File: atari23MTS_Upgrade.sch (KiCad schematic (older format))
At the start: 70 parts, among them P1 CONN_01X01, P10 CONN_01X01, P2 CONN_01X01, P3 CONN_01X01, P4 CONN_01X01, P5 CONN_01X01, P6 CONN_01X01, P7 CONN_01X01, P8 CONN_01X01, P9 CONN_01X01, SW1 SW_PUSH, SW2 SW_PUSH, U1 NCP1117ST33T3G, U2 STM32F401RCTx, U3 NCP1117ST33T3G, U4 STM32F401RCTx

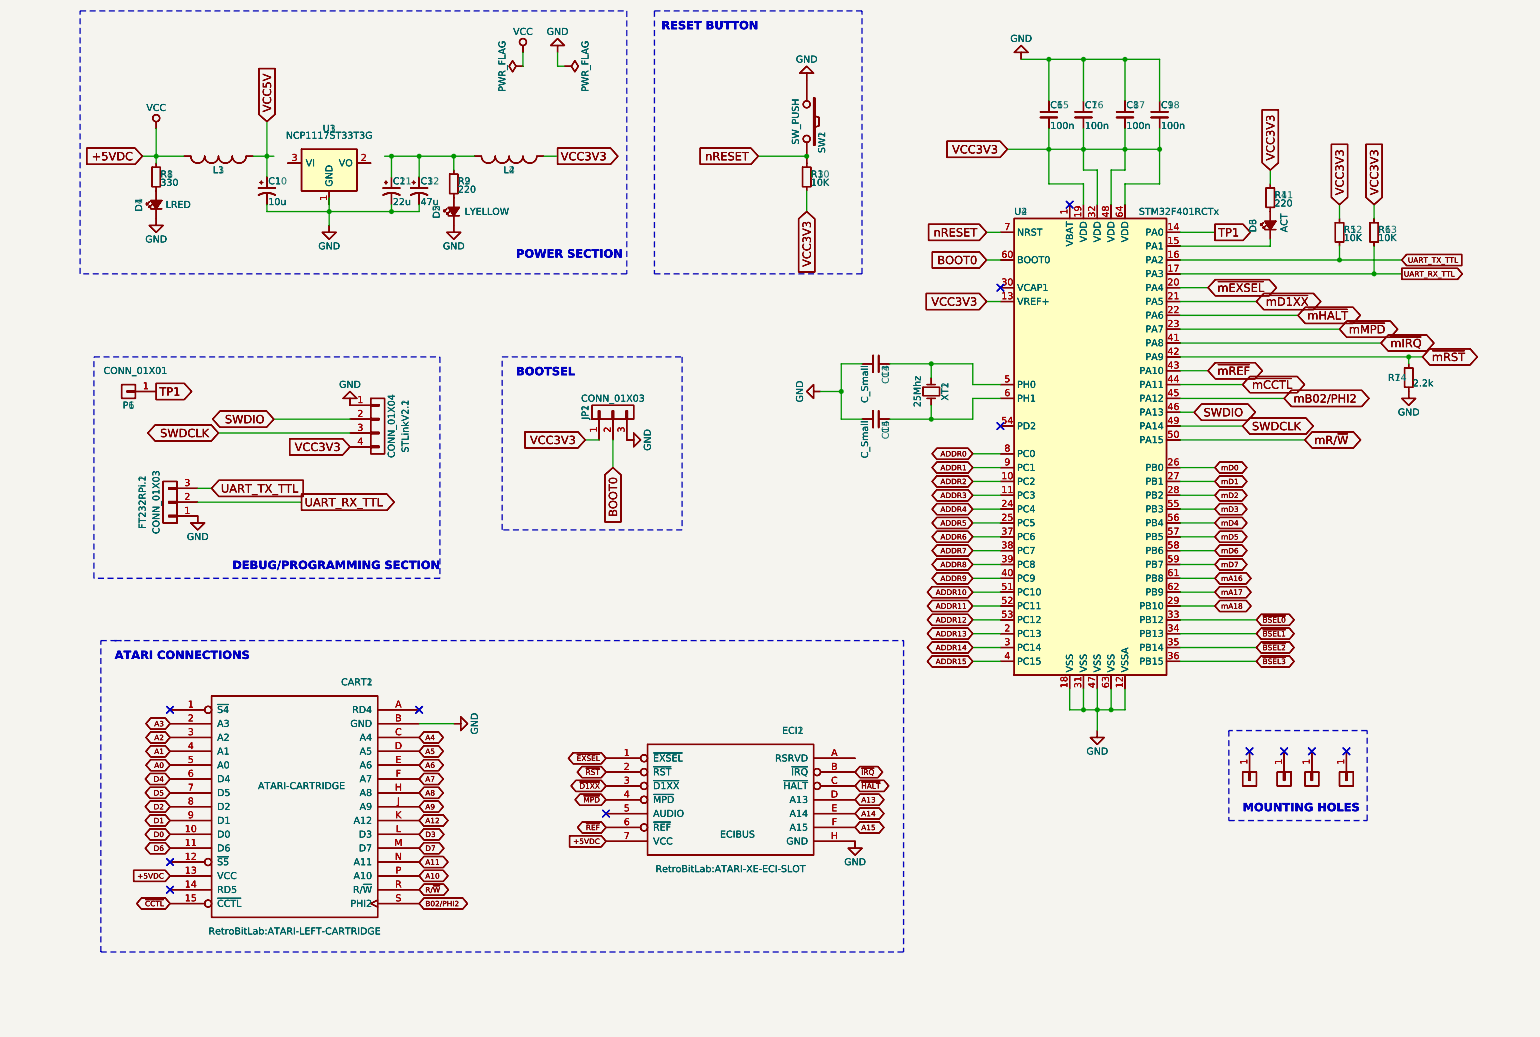
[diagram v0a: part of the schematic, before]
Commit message: added some footprint and revised logic for address selection
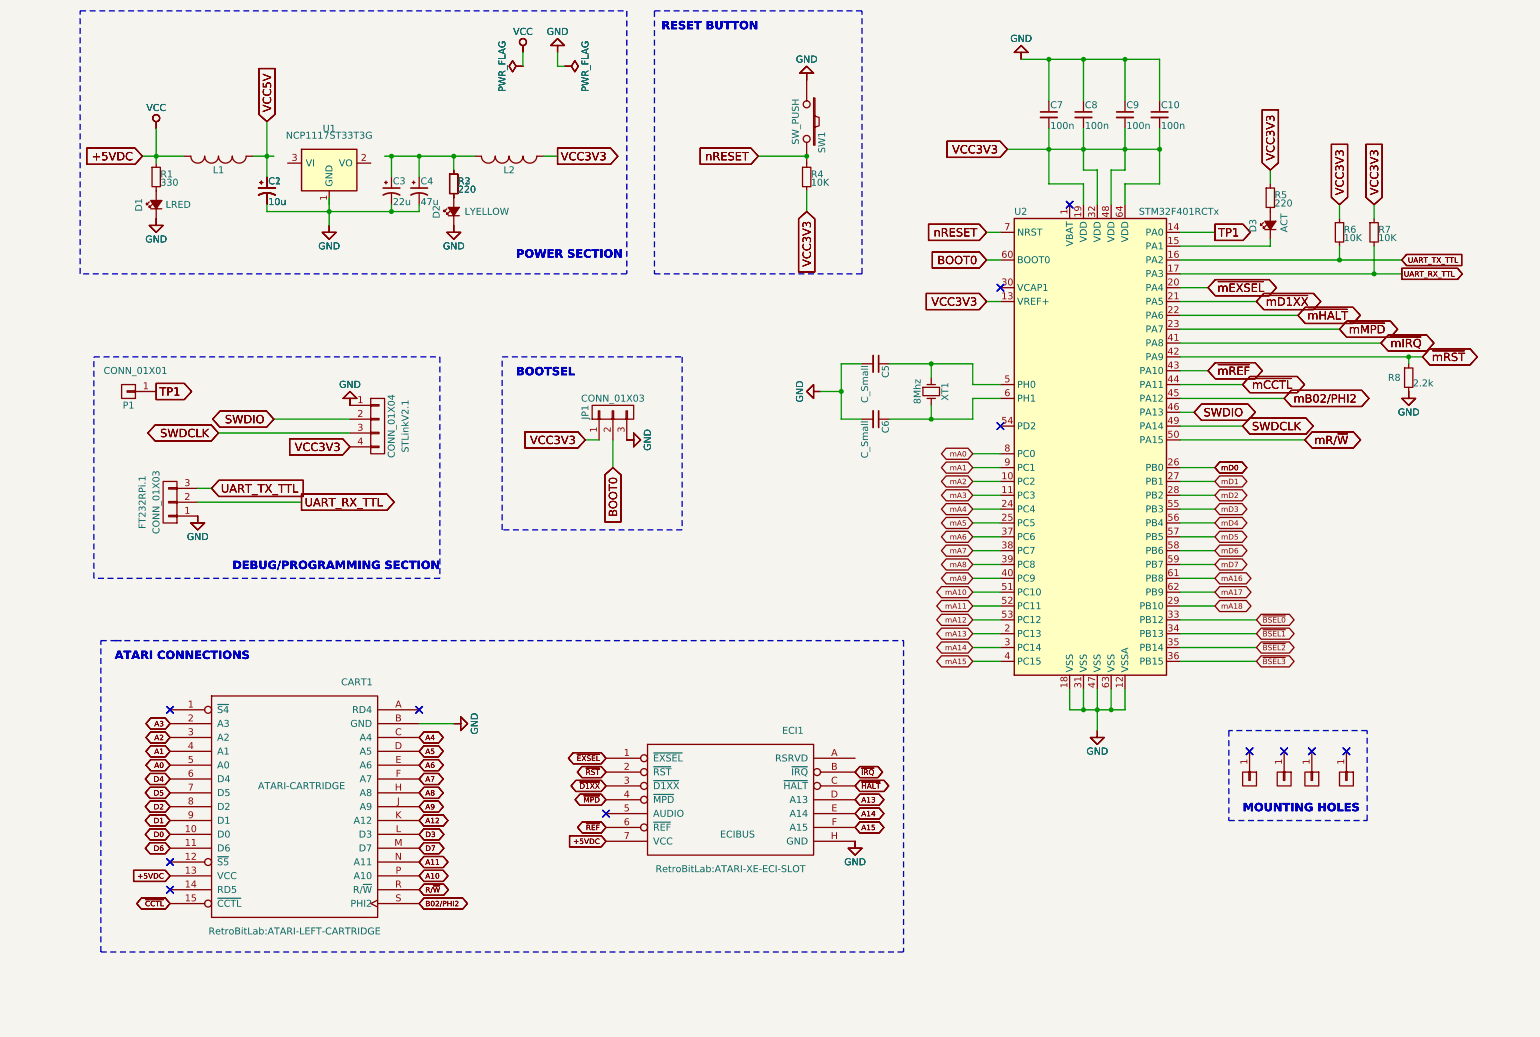
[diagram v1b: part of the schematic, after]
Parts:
- removed C11: 22u, Capacitors_SMD:c_elec_5x5.3, symbol CP1_Small
- removed C3: 47u, Capacitors_SMD:c_elec_5x5.3, symbol CP1_Small
- removed C4, C5: C_Small, Capacitors_SMD:C_1206_HandSoldering, symbol C_Small
- removed C6, C7, C8, C9: 100n, Capacitors_SMD:C_1206_HandSoldering, symbol C_Small
- removed CART1: ATARI-CARTRIDGE, RetroBitLab:ATARI-LEFT-CARTRIDGE, symbol ATARICARTRIDGE
- removed D1: LRED, LEDs:LED_1206, symbol Led_Small
- removed D2: LYELLOW, LEDs:LED_1206, symbol Led_Small
- removed D3: ACT, LEDs:LED_1206, symbol Led_Small
- removed ECI1: ECIBUS, RetroBitLab:ATARI-XE-ECI-SLOT, symbol ECIBUS
- removed FT232RPi.1, JP1: CONN_01X03, Pin_Headers:Pin_Header_Straight_1x03, symbol CONN_01X03
- removed L1, L2: INDUCTOR_SMALL, Choke_SMD:Choke_SMD_1206_Handsoldering, symbol INDUCTOR_SMALL
- removed P1: CONN_01X01, Measurement_Points:Measurement_Point_Round-SMD-Pad_Small, symbol CONN_01X01
- removed P2, P3, P4, P5: CONN_01X01, Connect:1pin, symbol CONN_01X01
- removed R1: 330, Resistors_SMD:R_1206_HandSoldering, symbol R_Small
- removed R3, R5, R6: 10K, Resistors_SMD:R_1206_HandSoldering, symbol R_Small
- removed R4: 220, Resistors_SMD:R_1206_HandSoldering, symbol R_Small
- removed R7: 2.2k, Resistors_SMD:R_1206_HandSoldering, symbol R_Small
- removed STLinkV2.1: CONN_01X04, Pin_Headers:Pin_Header_Angled_1x04, symbol CONN_01X04
- removed SW1: SW_PUSH, Buttons_Switches_SMD:SW_SPST_FSMSM, symbol SW_PUSH
- removed U1: NCP1117ST33T3G, TO_SOT_Packages_SMD:SOT-223, symbol NCP1117ST33T3G
- removed U2: STM32F401RCTx, Housings_QFP:LQFP-64_10x10mm_Pitch0.5mm, symbol STM32F401RCTx
- removed XT1: 25Mhz, Crystals:Crystal_SMD_0603_4Pads, symbol Crystal_Small
- XT1: renamed from XT2; value 25Mhz -> 8Mhz
- renumbered C18 to C10, C10 to C2, C2 to C3, C12 to C4, C13 to C5, C14 to C6, C15 to C7, C16 to C8, C17 to C9, CART2 to CART1, D4 to D1, D5 to D2, D6 to D3, ECI2 to ECI1, FT232RPi.2 to FT232RPi.1, JP2 to JP1, L3 to L1, L4 to L2, P6 to P1, P7 to P2, P8 to P3, P9 to P4, P10 to P5, R8 to R1, R9 to R3, R10 to R4, R11 to R5, R12 to R6, R13 to R7, R14 to R8, STLinkV2.2 to STLinkV2.1, SW2 to SW1, U3 to U1, U4 to U2
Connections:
- net ADDR0 renamed mA0
- net ADDR1 renamed mA1
- net ADDR10 renamed mA10
- net ADDR11 renamed mA11
- net ADDR12 renamed mA12
- net ADDR13 renamed mA13
- net ADDR14 renamed mA14
- net ADDR15 renamed mA15
- net ADDR2 renamed mA2
- net ADDR3 renamed mA3
- net ADDR4 renamed mA4
- net ADDR5 renamed mA5
- net ADDR6 renamed mA6
- net ADDR7 renamed mA7
- net ADDR8 renamed mA8
- net ADDR9 renamed mA9

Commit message: modified logic & added pcb
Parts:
- removed C1: 10u, Capacitors_SMD:c_elec_5x5.3, symbol CP1_Small
- removed R2: 220, Resistors_SMD:R_1206_HandSoldering, symbol R_Small
- added U3: 74LS138, Housings_SSOP:TSSOP-16_4.4x5mm_Pitch0.65mm, symbol 74LS138
- renumbered C2 to C1, C3 to C2, C4 to C3, C5 to C4, C6 to C5, C7 to C6, C8 to C7, C9 to C8, C10 to C9, R3 to R2, R4 to R3, R8 to R4
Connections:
- net mA16 is gone; now on net ~mEXSEL: U2.61 (PB8)
- net mA17 is gone; now on net ~mD1XX: U2.62 (PB9)
- net mA18 is gone; now on net ~mHALT: U2.29 (PB10)
- net GND: now also U3.8 (GND)
- net VCC3V3: now also U3.16 (VCC), U3.6 (E3)
- net mB02/PHI2: now also U2.54 (PD2); no longer U2.45 (PA12)
- net nRESET: now also R3.1, SW1.2
- net ~BSEL0: now also U3.15 (O0); no longer U2.33 (PB12)
- net ~BSEL1: now also U3.14 (O1); no longer U2.34 (PB13)
- net ~BSEL2: now also U3.13 (O2); no longer U2.35 (PB14)
- net ~BSEL3: now also U3.12 (O3); no longer U2.36 (PB15)
- net ~mCCTL: now also U2.45 (PA12); no longer U2.44 (PA11)
- net ~mD1XX: no longer U2.21 (PA5)
- net ~mEXSEL: no longer U2.20 (PA4)
- net ~mHALT: no longer U2.22 (PA6)
- net ~mIRQ: now also U2.34 (PB13); no longer U2.41 (PA8)
- net ~mMPD: now also U2.33 (PB12); no longer U2.23 (PA7)
- net ~mREF: now also U2.35 (PB14); no longer U2.43 (PA10)
- net ~mRST: now also U2.36 (PB15); no longer U2.42 (PA9)
- new net: U3.4 (E1), U3.5 (E2)
- new net PB0: U2.20 (PA4)
- new net PB1: U2.21 (PA5)
- new net PB2: U2.22 (PA6)
- new net PB3: U2.23 (PA7)
- new net PB4: U2.41 (PA8)
- new net PB5: U2.42 (PA9), U3.1 (A0)
- new net PB6: U2.43 (PA10), U3.2 (A1)
- new net PB7: U2.44 (PA11), U3.3 (A2)
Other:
- note added: "16K BANK SELECTORS"
- note added: "ADDRESS DECODER"
- moved on the sheet: C4, C5, R3, R4, XT1

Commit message: Important changes
Added extra symbols and update footprints for CARTRIDGE and ECI Bus
extender. Need a angled pcb to slots to be defined with spacers (pvc)
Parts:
- added EXTPWR1: CONN_01X04, Pin_Headers:Pin_Header_Angled_1x04, symbol CONN_01X04
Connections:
- net GND: now also EXTPWR1.2 (P2), EXTPWR1.3 (P3)
- net VCC: now also EXTPWR1.1 (P1)
- net ~S4: now reaches CART1.1 (~S4)
- net ~S5: now reaches CART1.12 (~S5)
- net RD5: now reaches CART1.14 (RD5)
- net RD4: now reaches CART1.A (RD4)
- net AUDIO: now reaches ECI1.5 (AUDIO)
- net RSRVD: now reaches ECI1.A (RSRVD)
- no-connect marks 24 -> 15
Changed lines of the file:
@@
 $Descr A4 11693 8268
 encoding utf-8
-Sheet 1 2
+Sheet 1 3
 Title "ATARI4MegExpansion"
 Date "2018-12-31"
@@
 	7800 5450 7800 5600
 Connection ~ 7800 5600
-NoConn ~ 1200 5600
-NoConn ~ 1200 6700
-NoConn ~ 1200 6900
-NoConn ~ 3000 5600
-NoConn ~ 4350 6350
 Wire Wire Line
 	3000 5700 3250 5700
@@
 	1    0    0    -1
 $EndComp
-NoConn ~ 1200 5600
-NoConn ~ 1200 6700
-NoConn ~ 1200 6900
-NoConn ~ 3000 5600
-NoConn ~ 4350 6350
 Text GLabel 1200 6800 0    39   Input ~ 0
 +5VDC
@@
 Text Notes 9750 4950 0    60   ~ 0
 ADDRESS DECODER
+$Comp
+L CONN_01X04 EXTPWR1
+U 1 1 5C2F33D4
+P 2750 950
+F 0 "EXTPWR1" V 2950 950 50  0000 C CNN
+F 1 "CONN_01X04" V 2850 950 50  0000 C CNN
+F 2 "Pin_Headers:Pin_Header_Angled_1x04" H 2750 950 50  0001 C CNN
+F 3 "" H 2750 950 50  0000 C CNN
+	1    2750 950
+	0    1    1    0
+$EndComp
+$Comp
+L GND #PWR023
+U 1 1 5C2F34E0
+P 2800 750
+F 0 "#PWR023" H 2800 500 50  0001 C CNN
+F 1 "GND" H 2700 600 50  0000 C CNN
+F 2 "" H 2800 750 50  0001 C CNN
+F 3 "" H 2800 750 50  0001 C CNN
+	1    2800 750
+	-1   0    0    1
+$EndComp
+$Comp
+L GND #PWR024
+U 1 1 5C2F354E
+P 2700 750
+F 0 "#PWR024" H 2700 500 50  0001 C CNN
+F 1 "GND" H 2800 600 50  0000 C CNN
+F 2 "" H 2700 750 50  0001 C CNN
+F 3 "" H 2700 750 50  0001 C CNN
+	1    2700 750
+	-1   0    0    1
+$EndComp
+NoConn ~ 2600 750
+Text GLabel 3000 750  2    39   BiDi ~ 0
++5VDC
+Wire Wire Line
+	3000 750  2900 750
+$Sheet
+S 50   17500 11650 8350
+U 5C2FF215
+F0 "Expansion Slots pass through" 39
+F1 "expansionslotspt.sch" 39
+$EndSheet
+Text GLabel 6150 5950 2    39   BiDi ~ 0
+RSRVD
+Text GLabel 4350 6350 0    39   BiDi ~ 0
+AUDIO
+Text GLabel 3000 5600 2    39   BiDi ~ 0
+RD4
+Text GLabel 1200 5600 0    39   BiDi ~ 0
+~S4
+Text GLabel 1200 6700 0    39   BiDi ~ 0
+~S5
+Text GLabel 1200 6900 0    39   BiDi ~ 0
+RD5
 $EndSCHEMATC

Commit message: Revised logic using nOE and R/nW as supposed to be...
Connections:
- net ~ADDRSEL16K: now reaches U3.4 (E1), U3.5 (E2)
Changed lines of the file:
@@
 encoding utf-8
 Sheet 1 3
-Title "ATARI4MegExpansion"
+Title "ATARI XE 2/4 MegaRAM Expansion"
 Date "2018-12-31"
 Rev ""
@@
 NoConn ~ 10700 4150
 NoConn ~ 10700 4250
-Wire Wire Line
-	9700 4150 9700 4500
-Wire Wire Line
-	9700 4500 10200 4500
-Connection ~ 9700 4250
-Connection ~ 10200 4500
-Text GLabel 9700 4050 0    60   Input ~ 0
-VCC3V3
 Text GLabel 9700 3550 0    39   BiDi ~ 0
 PB5
@@
 Text GLabel 1200 6900 0    39   BiDi ~ 0
 RD5
+Text GLabel 9700 4150 0    39   BiDi ~ 0
+~ADDRSEL16K
+Text GLabel 9700 4250 0    39   BiDi ~ 0
+~ADDRSEL16K
+Text GLabel 9700 4050 0    39   Input ~ 0
+VCC3V3
 $EndSCHEMATC

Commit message: Added logos & GND Pin for electrical debugging
Added Atari Logo on the back
Added GNU GPL on Silkscreen Top
Added Test Point for GROUND (do not place in production)
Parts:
- added DISABLE.MODE.1: CONN_01X02, Pin_Headers:Pin_Header_Straight_1x02, symbol CONN_01X02
- added P6: CONN_01X01, Pin_Headers:Pin_Header_Straight_1x01, symbol CONN_01X01
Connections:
- net GND: now also DISABLE.MODE.1.2 (P2), P6.1 (P1)
- net nRESET: now also DISABLE.MODE.1.1 (P1)
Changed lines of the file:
@@
 Text GLabel 9700 4050 0    39   Input ~ 0
 VCC3V3
+$Comp
+L CONN_01X01 P6
+U 1 1 5C326A2F
+P 1050 850
+F 0 "P6" H 1050 950 50  0000 C CNN
+F 1 "CONN_01X01" H 1000 700 50  0000 C CNN
+F 2 "Pin_Headers:Pin_Header_Straight_1x01" H 1050 850 50  0001 C CNN
+F 3 "" H 1050 850 50  0000 C CNN
+	1    1050 850
+	-1   0    0    1
+$EndComp
+Text GLabel 1400 850  2    60   Output ~ 0
+GND
+$Comp
+L GND #PWR025
+U 1 1 5C3272A9
+P 1250 850
+F 0 "#PWR025" H 1250 600 50  0001 C CNN
+F 1 "GND" H 1250 700 50  0000 C CNN
+F 2 "" H 1250 850 50  0001 C CNN
+F 3 "" H 1250 850 50  0001 C CNN
+	1    1250 850
+	1    0    0    -1
+$EndComp
+Wire Wire Line
+	1400 850  1250 850
+Wire Wire Line
+	5550 1300 5550 1700
+Connection ~ 5550 1700
+$Comp
+L GND #PWR026
+U 1 1 5C32789C
+P 5550 1050
+F 0 "#PWR026" H 5550 800 50  0001 C CNN
+F 1 "GND" H 5550 900 50  0000 C CNN
+F 2 "" H 5550 1050 50  0001 C CNN
+F 3 "" H 5550 1050 50  0001 C CNN
+	1    5550 1050
+	-1   0    0    1
+$EndComp
+$Comp
+L CONN_01X02 DISABLE.MODE.1
+U 1 1 5C3278F4
+P 5350 1250
+F 0 "DISABLE.MODE.1" V 5550 1250 50  0000 C CNN
+F 1 "CONN_01X02" V 5450 1250 50  0000 C CNN
+F 2 "Pin_Headers:Pin_Header_Straight_1x02" H 5350 1250 50  0001 C CNN
+F 3 "" H 5350 1250 50  0000 C CNN
+	1    5350 1250
+	-1   0    0    1
+$EndComp
+Wire Wire Line
+	5550 1200 5550 1050
 $EndSCHEMATC

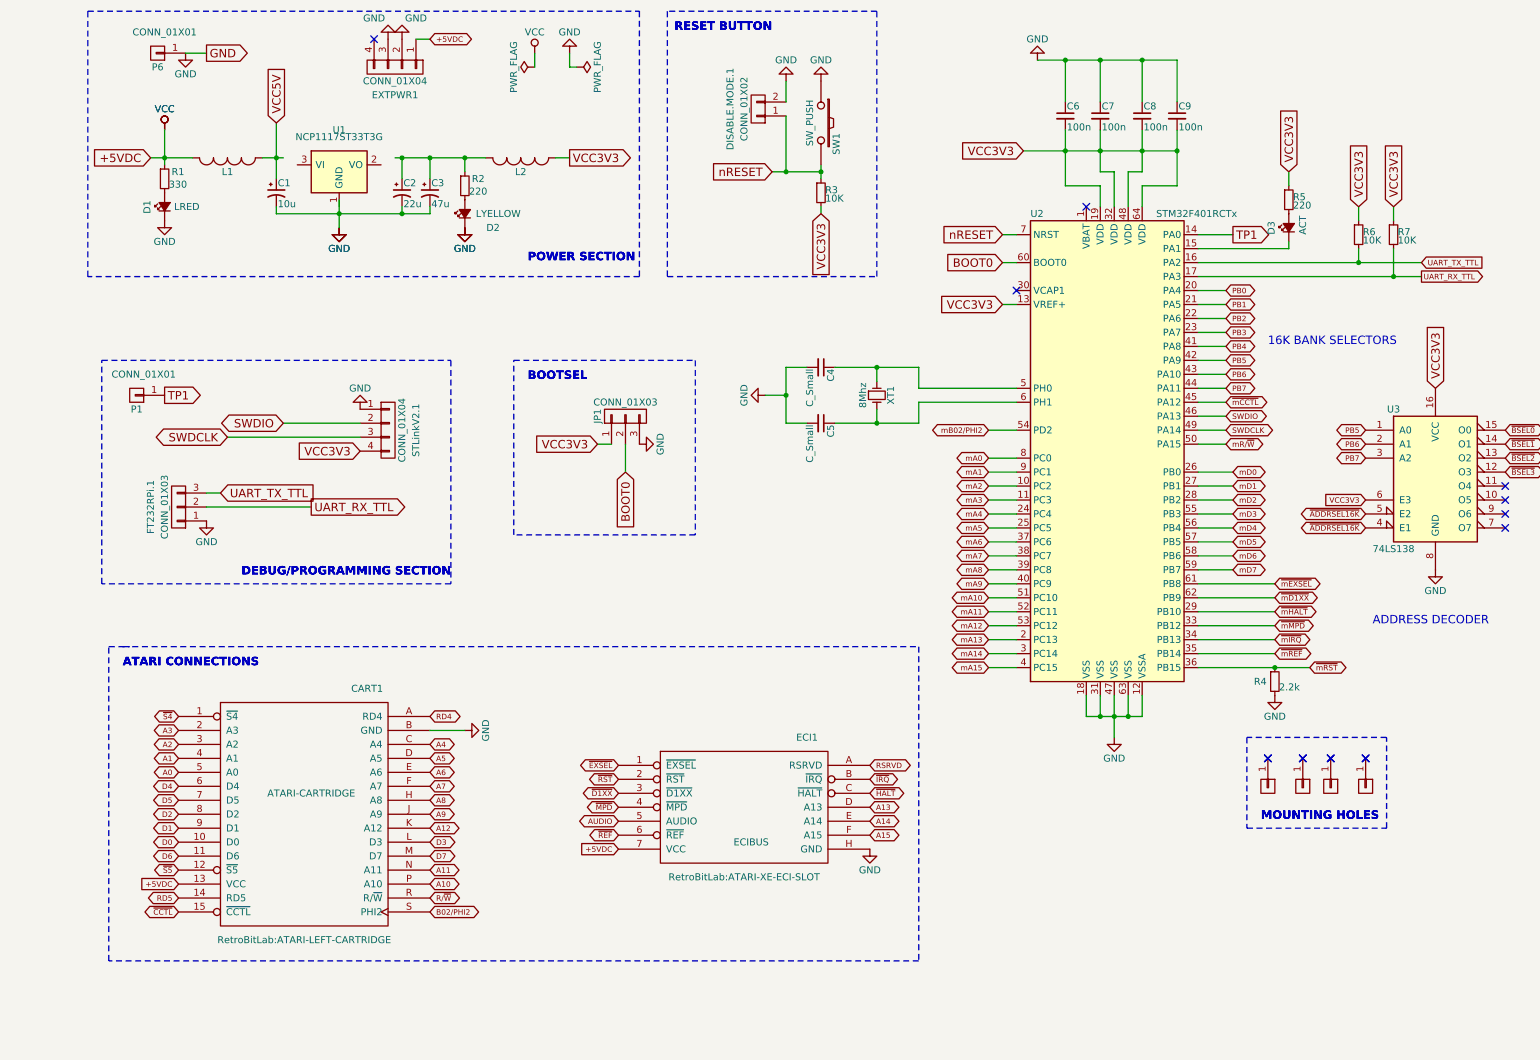
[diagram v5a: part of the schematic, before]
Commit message: Added resistor partitioner for mRST and Chip Enable for DECODER
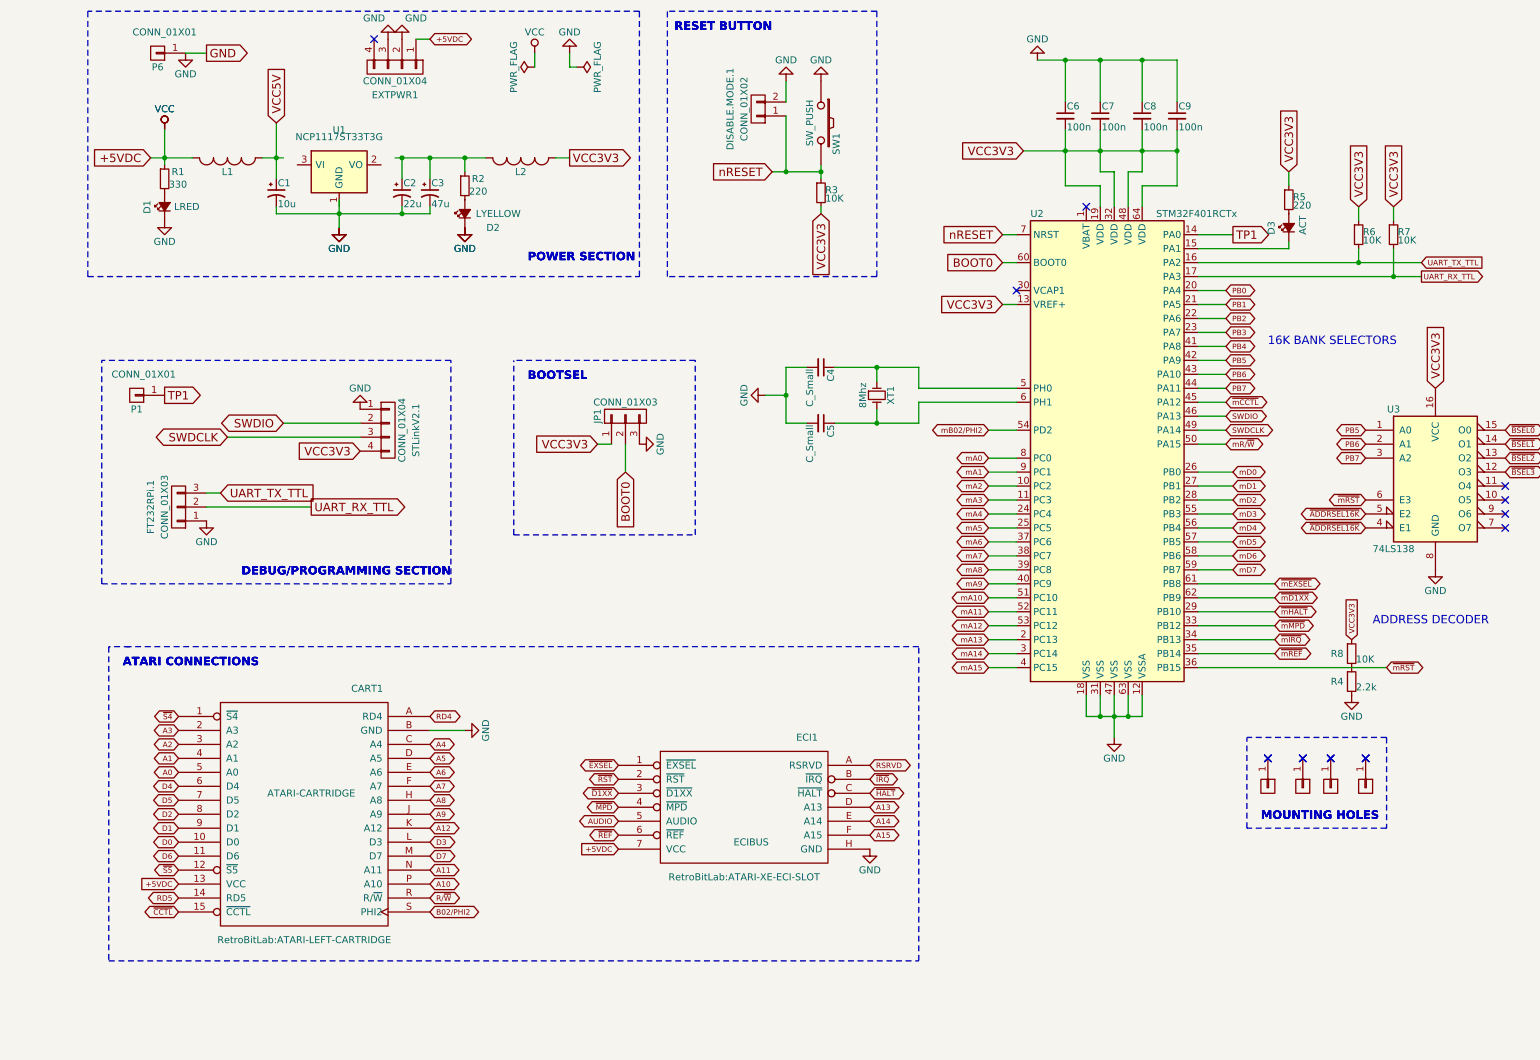
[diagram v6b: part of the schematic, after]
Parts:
- added R8: 10K, Resistors_SMD:R_1206_HandSoldering, symbol R_Small
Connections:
- net VCC3V3: now also R8.1; no longer U3.6 (E3)
- net ~mRST: now also U3.6 (E3); no longer R4.1
- new net: R4.1, R8.2
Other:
- moved on the sheet: R4
